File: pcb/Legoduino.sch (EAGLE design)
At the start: 91 parts, among them CON11 ISP-AVR, CON2 PIN(1+16)X3_DS, IC1 NCP3170ADR2G, IC2 RN-42, IC3 MIC5205-5.0YM5, IC4 ATMEGA2560-16AU, IC5 UG-2864HSWEG01_SPI, IC6 MIC5205-3.6YM5, IC7 MIC5205-3.3YM5, IC8 BD6221F-E2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

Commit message: Updated feedback compensation circuit for NCP3170
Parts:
- C10: value * -> 150p
- R15: value * -> 1k
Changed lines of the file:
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@@
 <grid distance="100" unitdist="mil" unit="mil" style="lines" multiple="1" display="no" altdistance="25" altunitdist="mil" altunit="mil"/>
 <layers>
-<layer number="1" name="Top" color="4" fill="1" visible="yes" active="no"/>
-<layer number="16" name="Bottom" color="1" fill="1" visible="yes" active="no"/>
-<layer number="17" name="Pads" color="2" fill="1" visible="yes" active="no"/>
-<layer number="18" name="Vias" color="2" fill="1" visible="yes" active="no"/>
-<layer number="19" name="Unrouted" color="6" fill="1" visible="yes" active="no"/>
-<layer number="20" name="Dimension" color="15" fill="1" visible="yes" active="no"/>
-<layer number="21" name="tPlace" color="7" fill="1" visible="yes" active="no"/>
-<layer number="22" name="bPlace" color="7" fill="1" visible="yes" active="no"/>
-<layer number="23" name="tOrigins" color="15" fill="1" visible="yes" active="no"/>
-<layer number="24" name="bOrigins" color="15" fill="1" visible="yes" active="no"/>
-<layer number="25" name="tNames" color="7" fill="1" visible="yes" active="no"/>
-<layer number="26" name="bNames" color="7" fill="1" visible="yes" active="no"/>
-<layer number="27" name="tValues" color="7" fill="1" visible="yes" active="no"/>
-<layer number="28" name="bValues" color="7" fill="1" visible="yes" active="no"/>
+<layer number="1" name="Top" color="4" fill="1" visible="no" active="no"/>
+<layer number="16" name="Bottom" color="1" fill="1" visible="no" active="no"/>
+<layer number="17" name="Pads" color="2" fill="1" visible="no" active="no"/>
+<layer number="18" name="Vias" color="2" fill="1" visible="no" active="no"/>
+<layer number="19" name="Unrouted" color="6" fill="1" visible="no" active="no"/>
+<layer number="20" name="Dimension" color="15" fill="1" visible="no" active="no"/>
+<layer number="21" name="tPlace" color="7" fill="1" visible="no" active="no"/>
+<layer number="22" name="bPlace" color="7" fill="1" visible="no" active="no"/>
+<layer number="23" name="tOrigins" color="15" fill="1" visible="no" active="no"/>
+<layer number="24" name="bOrigins" color="15" fill="1" visible="no" active="no"/>
+<layer number="25" name="tNames" color="7" fill="1" visible="no" active="no"/>
+<layer number="26" name="bNames" color="7" fill="1" visible="no" active="no"/>
+<layer number="27" name="tValues" color="7" fill="1" visible="no" active="no"/>
+<layer number="28" name="bValues" color="7" fill="1" visible="no" active="no"/>
 <layer number="29" name="tStop" color="7" fill="3" visible="no" active="no"/>
 <layer number="30" name="bStop" color="7" fill="6" visible="no" active="no"/>
@@
 <layer number="35" name="tGlue" color="7" fill="4" visible="no" active="no"/>
 <layer number="36" name="bGlue" color="7" fill="5" visible="no" active="no"/>
-<layer number="37" name="tTest" color="7" fill="1" visible="yes" active="no"/>
-<layer number="38" name="bTest" color="7" fill="1" visible="yes" active="no"/>
+<layer number="37" name="tTest" color="7" fill="1" visible="no" active="no"/>
+<layer number="38" name="bTest" color="7" fill="1" visible="no" active="no"/>
 <layer number="39" name="tKeepout" color="4" fill="11" visible="no" active="no"/>
 <layer number="40" name="bKeepout" color="1" fill="11" visible="no" active="no"/>
@@
 <layer number="44" name="Drills" color="7" fill="1" visible="no" active="no"/>
 <layer number="45" name="Holes" color="7" fill="1" visible="no" active="no"/>
-<layer number="46" name="Milling" color="3" fill="1" visible="yes" active="no"/>
-<layer number="47" name="Measures" color="7" fill="1" visible="yes" active="no"/>
-<layer number="48" name="Document" color="7" fill="1" visible="yes" active="no"/>
-<layer number="49" name="Reference" color="12" fill="1" visible="yes" active="no"/>
-<layer number="50" name="dxf" color="12" fill="1" visible="yes" active="no"/>
-<layer number="51" name="tDocu" color="7" fill="11" visible="yes" active="no"/>
-<layer number="52" name="bDocu" color="7" fill="11" visible="yes" active="no"/>
-<layer number="53" name="tGND_GNDA" color="7" fill="1" visible="yes" active="no"/>
-<layer number="54" name="bGND_GNDA" color="7" fill="1" visible="yes" active="no"/>
-<layer number="56" name="wert" color="7" fill="1" visible="yes" active="no"/>
+<layer number="46" name="Milling" color="3" fill="1" visible="no" active="no"/>
+<layer number="47" name="Measures" color="7" fill="1" visible="no" active="no"/>
+<layer number="48" name="Document" color="7" fill="1" visible="no" active="no"/>
+<layer number="49" name="Reference" color="12" fill="1" visible="no" active="no"/>
+<layer number="50" name="dxf" color="12" fill="1" visible="no" active="no"/>
+<layer number="51" name="tDocu" color="7" fill="11" visible="no" active="no"/>
+<layer number="52" name="bDocu" color="7" fill="11" visible="no" active="no"/>
+<layer number="53" name="tGND_GNDA" color="7" fill="1" visible="no" active="no"/>
+<layer number="54" name="bGND_GNDA" color="7" fill="1" visible="no" active="no"/>
+<layer number="56" name="wert" color="7" fill="1" visible="no" active="no"/>
 <layer number="91" name="Nets" color="2" fill="1" visible="yes" active="yes"/>
 <layer number="92" name="Busses" color="1" fill="1" visible="yes" active="yes"/>
@@
 <part name="GND11" library="PN_default" deviceset="GND" device=""/>
 <part name="GND15" library="PN_default" deviceset="GND" device=""/>
-<part name="R15" library="PN_default" deviceset="R" device="0603" value="*"/>
-<part name="C10" library="PN_default" deviceset="C" device="0603" value="*"/>
+<part name="R15" library="PN_default" deviceset="R" device="0603" value="1k"/>
+<part name="C10" library="PN_default" deviceset="C" device="0603" value="150p"/>
 <part name="C11" library="PN_default" deviceset="C" device="1206" value="22u"/>
 <part name="GND16" library="PN_default" deviceset="GND" device=""/>

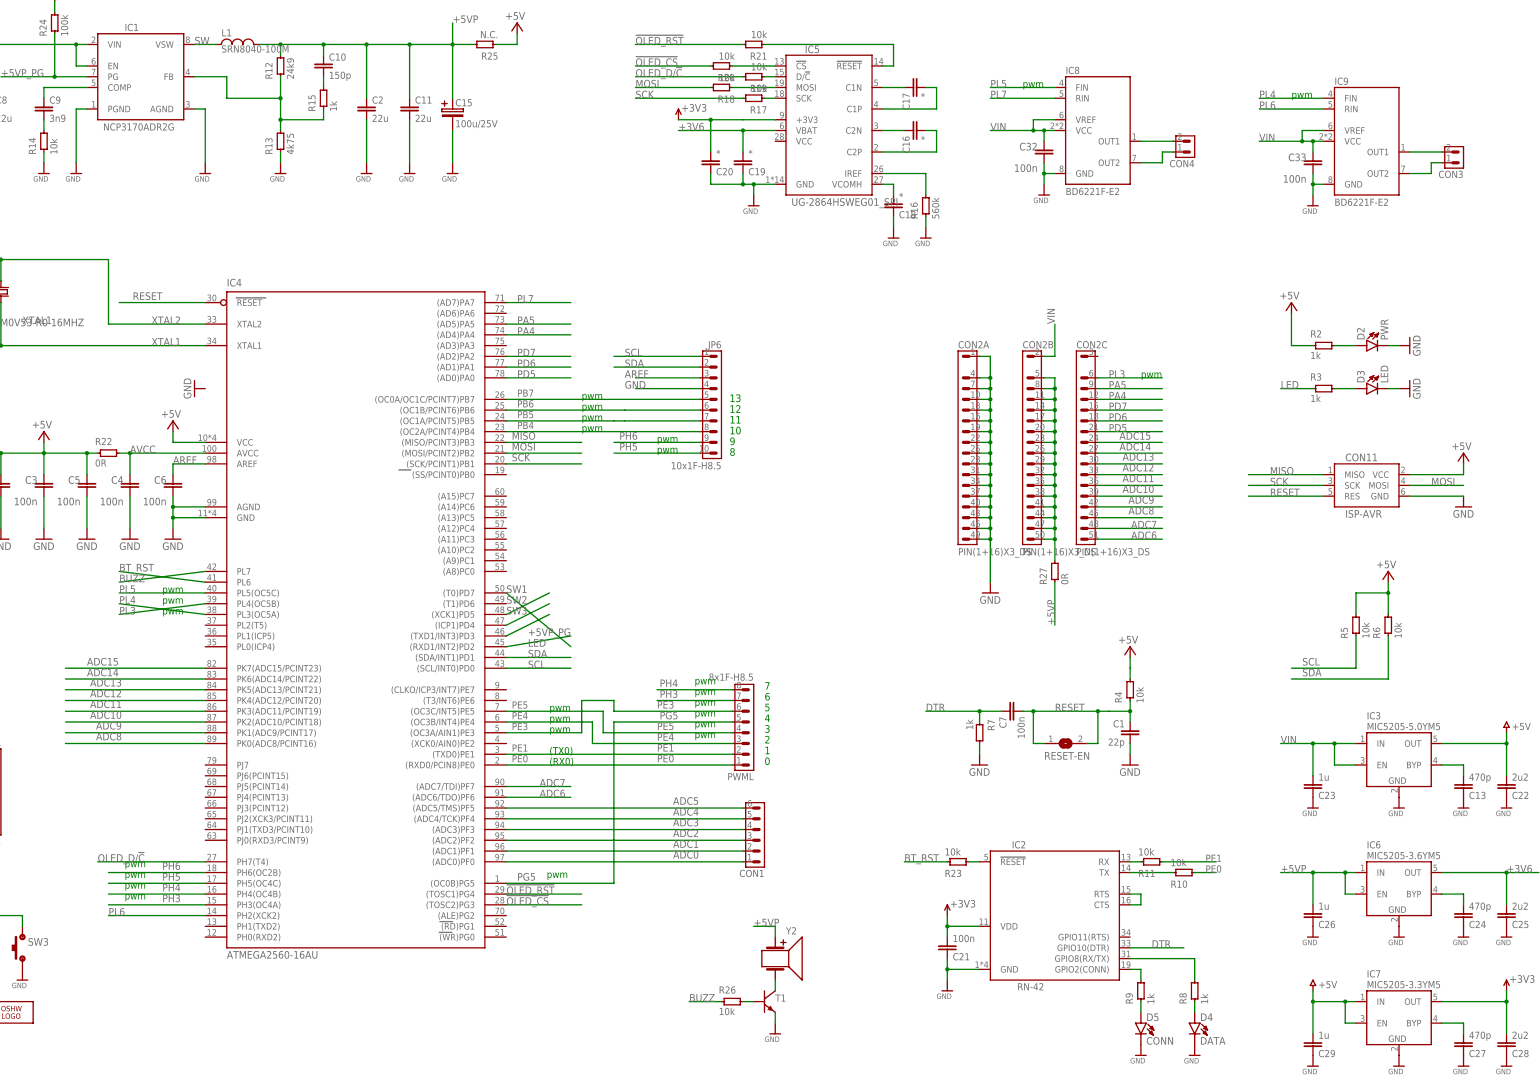
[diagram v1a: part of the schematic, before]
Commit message: Updated net names according to Arduino Mega pin numbers
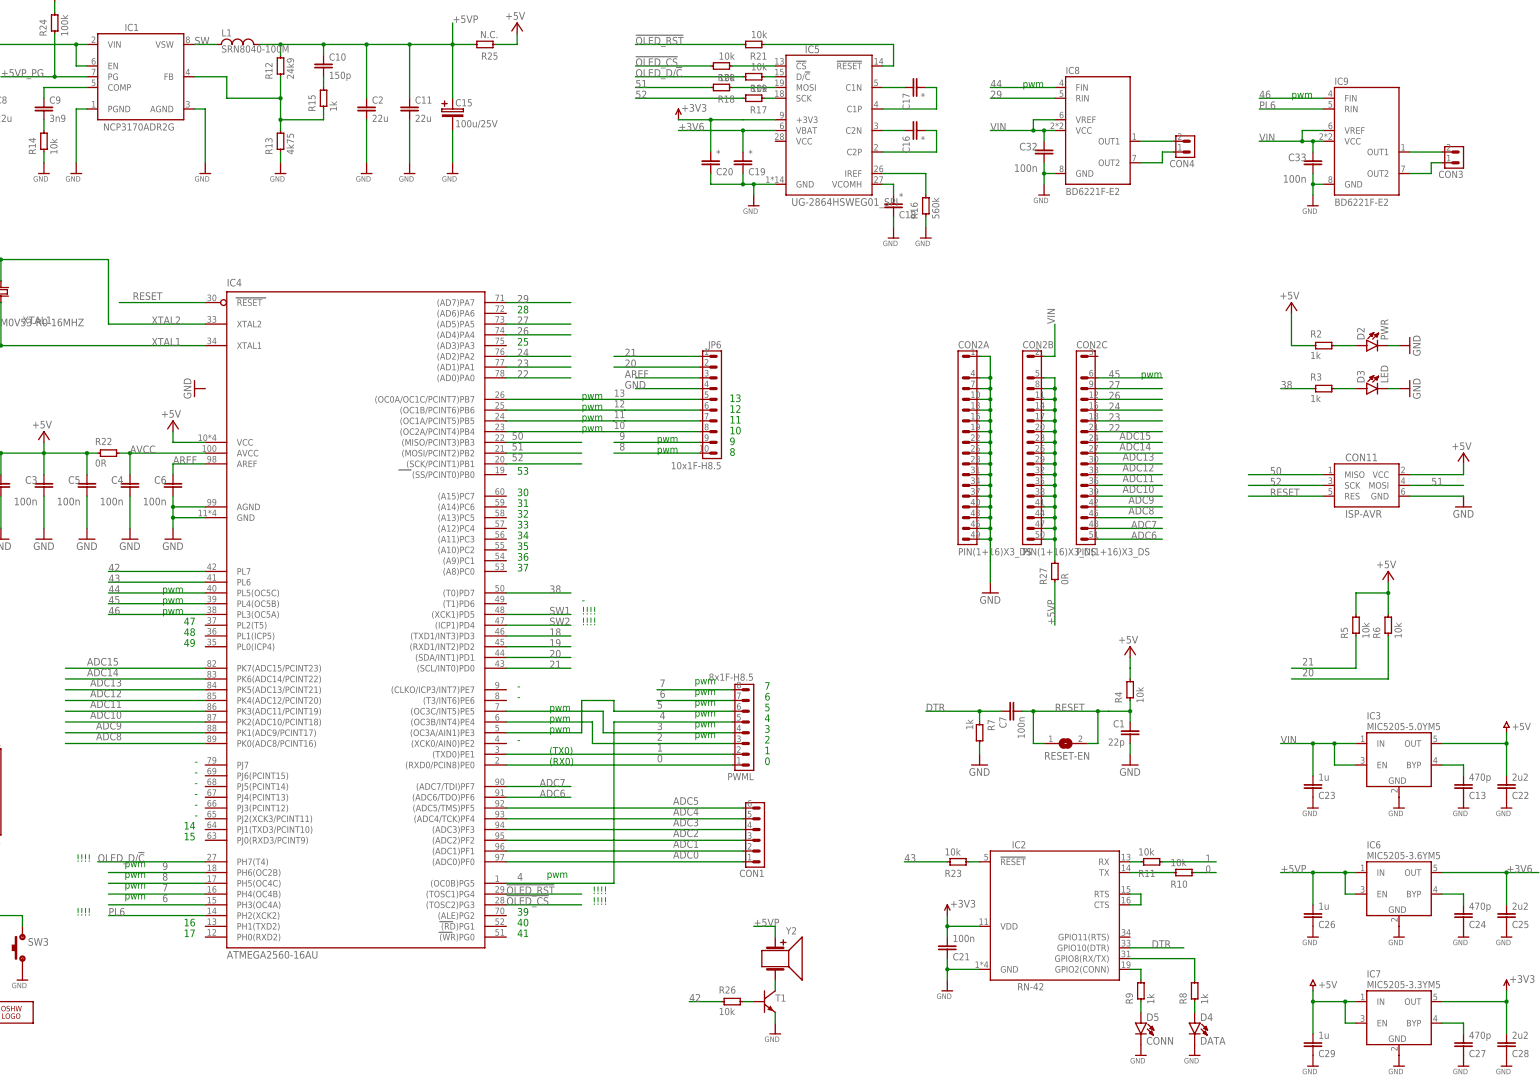
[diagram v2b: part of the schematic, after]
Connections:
- net BT_RST renamed 43
- net BUZZ renamed 42
- net LED renamed 38
- net MISO renamed 50
- net MOSI renamed 51
- net PA4 renamed 26
- net PA5 renamed 27
- net PB4 renamed 10
- net PB5 renamed 11
- net PB6 renamed 12
- net PB7 renamed 13
- net PD5 renamed 22
- net PD6 renamed 23
- net PD7 renamed 24
- net PE0 renamed 0
- net PE1 renamed 1
- net PE3 renamed 5
- net PE4 renamed 2
- net PE5 renamed 3
- net PG5 renamed 4
- net PH3 renamed 6
- net PH4 renamed 7
- net PH5 renamed 8
- net PH6 renamed 9
- net PL3 renamed 45
- net PL4 renamed 46
- net PL5 renamed 44
- net PL7 renamed 29
- net SCK renamed 52
- net SCL renamed 21
- net SDA renamed 20
- new net 18: IC4.(TXD1/INT3)PD3
- new net 19: IC4.(RXD1/INT2)PD2
- net +5VP_PG: no longer IC4.(RXD1/INT2)PD2
- net SW3: no longer IC4.(TXD1/INT3)PD3
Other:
- note added: "!!!!"
- note added: "-"
- note added: "14"
- note added: "15"
- note added: "16"
- note added: "17"
- note added: "25"
- note added: "28"
- note added: "30"
- note added: "31"
- note added: "32"
- note added: "33"
- note added: "34"
- note added: "35"
- note added: "36"
- note added: "37"
- note added: "39"
- note added: "40"
- note added: "41"
- note added: "47"
- note added: "48"
- note added: "49"
- note added: "53"
